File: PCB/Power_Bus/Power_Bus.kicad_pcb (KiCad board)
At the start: 2 copper layers, 64.8 x 30.5 mm, 42 parts, among them J1 CONN_01X01, J2 CONN_01X01, J3 CONN_01X01, J4 CONN_01X01, J5 D1306, J6 D1306, Q1 MMBT3904, Q2 TP0610T, Q3 Q_PMOS_GDS, Q4 TP0610T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

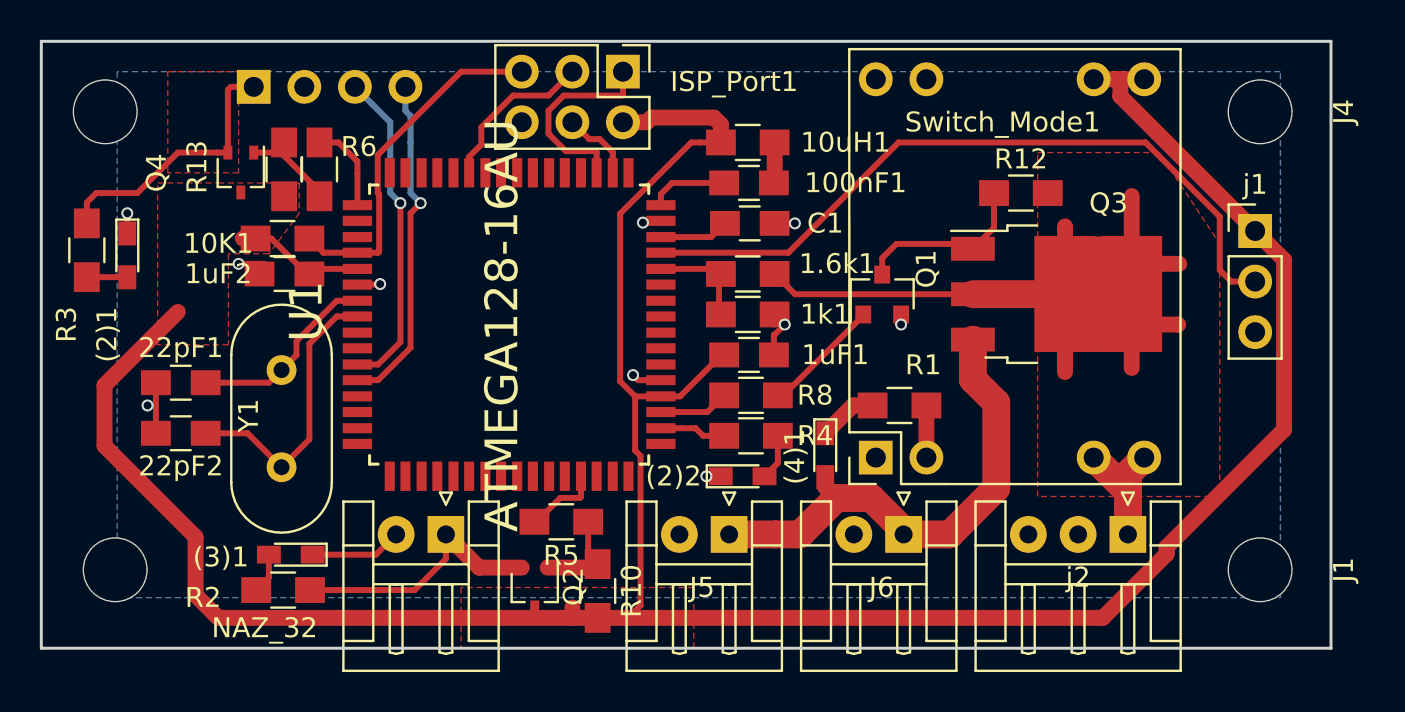
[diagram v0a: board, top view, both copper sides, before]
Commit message: added team name to silkscreen
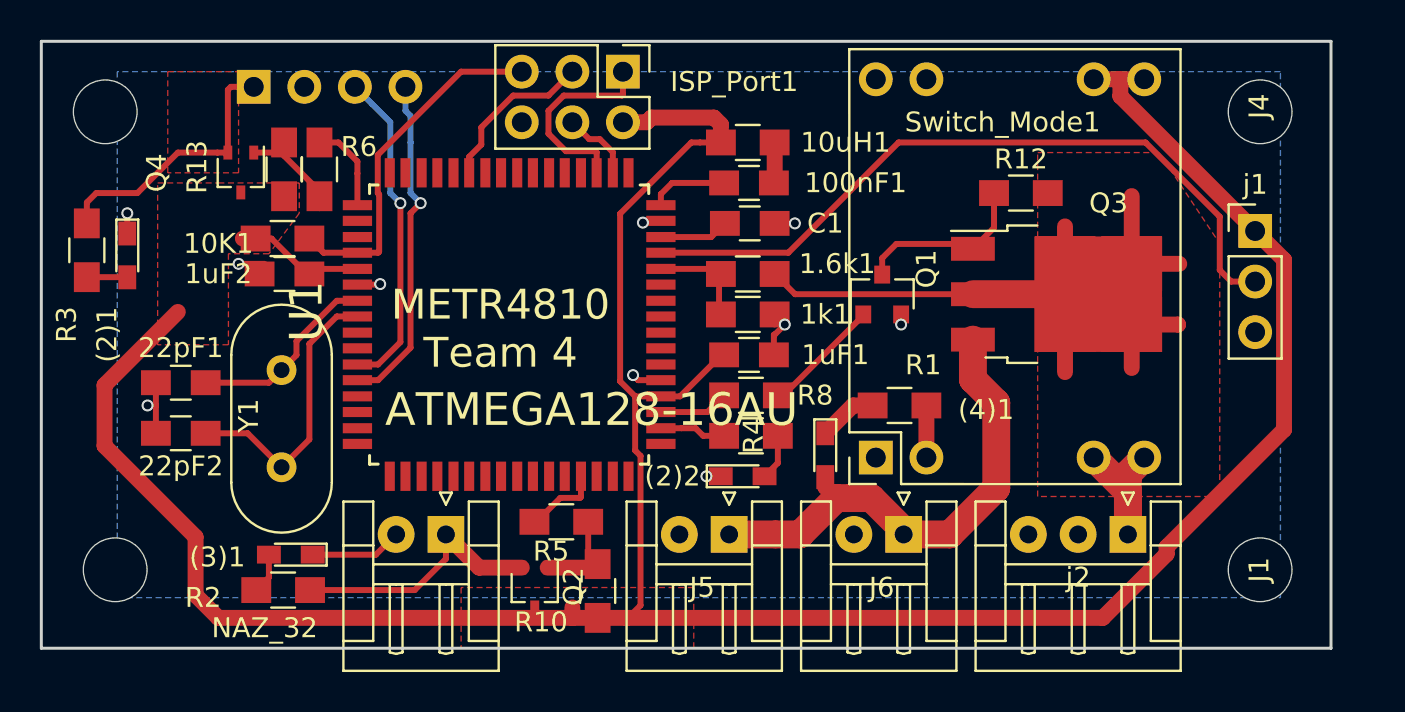
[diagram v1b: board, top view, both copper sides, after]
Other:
- board text added: "METR4810 Team 4"
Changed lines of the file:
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@@
     (links 86)
     (no_connects 0)
-    (area 60.884999 91.364999 91.515001 156.285001)
+    (area 70.984129 67.441069 138.061512 103.729189)
     (thickness 1.6)
-    (drawings 4)
+    (drawings 5)
     (tracks 248)
     (zones 0)
@@
   )
   (setup
-    (last_trace_width 1.4)
+    (last_trace_width 0.25)
     (user_trace_width 0.3)
     (user_trace_width 0.8)
@@
     (visible_elements 7FFFFFFF)
     (pcbplotparams
-      (layerselection 0x00030_80000001)
-      (usegerberextensions false)
+      (layerselection 0x010f0_80000001)
+      (usegerberextensions true)
       (excludeedgelayer true)
       (linewidth 0.100000)
@@
       (outputformat 1)
       (mirror false)
-      (drillshape 1)
+      (drillshape 0)
       (scaleselection 1)
       (outputdirectory ""))
@@
     (tags "resistor 0805")
     (attr smd)
-    (fp_text reference R5 (at 0 -1.7 180) (layer F.SilkS)
+    (fp_text reference R5 (at 0.512129 -1.484811 180) (layer F.SilkS)
       (effects (font (size 1 1) (thickness 0.15)))
     )
@@
       (effects (font (size 1.64342 1.64342) (thickness 0.05)))
     )
-    (fp_text value ATMEGA128-16AU (at 0.049629 0.355749 270) (layer F.SilkS)
+    (fp_text value ATMEGA128-16AU (at 4.278811 -4.139871 360) (layer F.SilkS)
       (effects (font (size 1.64293 1.64293) (thickness 0.05)))
     )
@@
     (tags "mounting hole 3.2mm no annular m3")
     (attr virtual)
-    (fp_text reference J1 (at 0 -4.2 270) (layer F.SilkS)
+    (fp_text reference J1 (at 0 0.047129 270) (layer F.SilkS)
       (effects (font (size 1 1) (thickness 0.15)))
     )
@@
     (tags "mounting hole 3.2mm no annular m3")
     (attr virtual)
-    (fp_text reference J4 (at 0 -4.2 270) (layer F.SilkS)
+    (fp_text reference J4 (at -0.277189 0.047129 270) (layer F.SilkS)
       (effects (font (size 1 1) (thickness 0.15)))
     )
@@
     (tags "resistor 0805")
     (attr smd)
-    (fp_text reference R4 (at 3.222 0) (layer F.SilkS)
+    (fp_text reference R4 (at 0.122871 0 90) (layer F.SilkS)
       (effects (font (size 1 1) (thickness 0.15)))
     )
@@
     (tags "resistor 0805")
     (attr smd)
-    (fp_text reference R10 (at 0 -1.7 270) (layer F.SilkS)
+    (fp_text reference R10 (at 1.564811 2.845129 540) (layer F.SilkS)
       (effects (font (size 1 1) (thickness 0.15)))
     )
@@
     (tags "LED 0603")
     (attr smd)
-    (fp_text reference "(2)2" (at -3.472 0) (layer F.SilkS)
+    (fp_text reference "(2)2" (at -3.523129 0) (layer F.SilkS)
       (effects (font (size 1 1) (thickness 0.15)))
     )
@@
     (tags "LED 0603")
     (attr smd)
-    (fp_text reference "(3)1" (at 3.513 -0.127 180) (layer F.SilkS)
+    (fp_text reference "(3)1" (at 3.691129 -0.127 180) (layer F.SilkS)
       (effects (font (size 1 1) (thickness 0.15)))
     )
@@
     (tags "LED 0603")
     (attr smd)
-    (fp_text reference "(4)1" (at 0.084 1.524 270) (layer F.SilkS)
+    (fp_text reference "(4)1" (at -2.282189 -8.076871 360) (layer F.SilkS)
       (effects (font (size 1 1) (thickness 0.15)))
     )
@@
     )
   )
+  (gr_text "METR4810\nTeam 4" (at 96.012 84.328) (layer F.SilkS)
+    (effects (font (size 1.5 1.5) (thickness 0.3)))
+  )
   (gr_line (start 137.719129 100.369189) (end 137.719129 69.889189) (layer Edge.Cuts) (width 0.15))
